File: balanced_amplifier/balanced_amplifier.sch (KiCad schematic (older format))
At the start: 2 parts

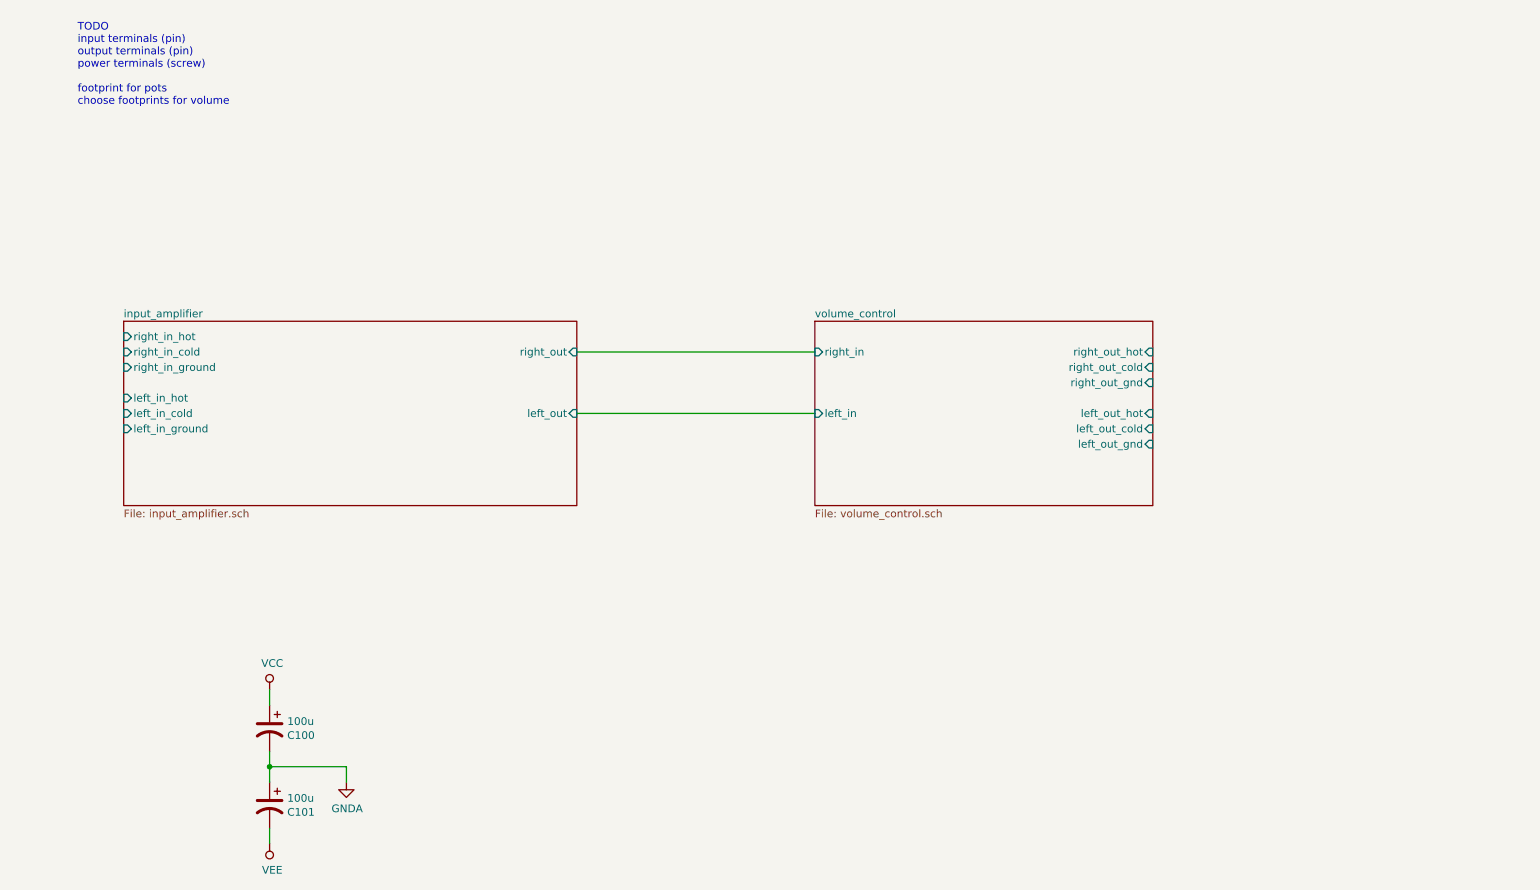
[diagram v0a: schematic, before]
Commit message: Add connectors to root sheet. Connector footprints may need to be changed
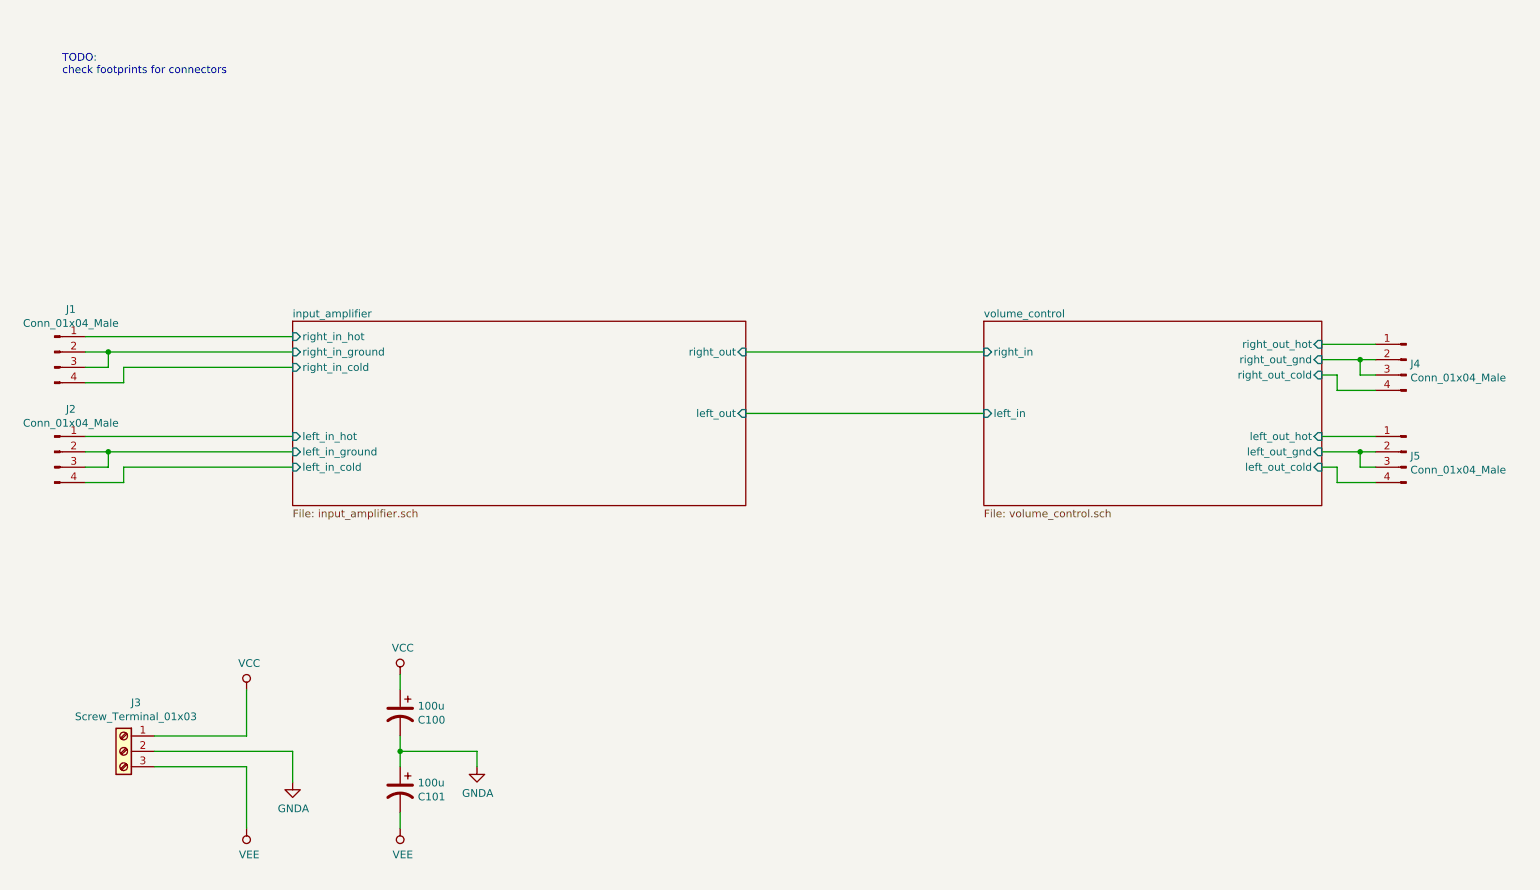
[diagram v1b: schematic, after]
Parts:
- added J1, J2, J4, J5: Conn_01x04_Male, Connector_PinHeader_2.54mm:PinHeader_1x04_P2.54mm_Vertical, symbol Connector:Conn_01x04_Male
- added J3: Screw_Terminal_01x03, TerminalBlock_Phoenix:TerminalBlock_Phoenix_MPT-0,5-3-2.54_1x03_P2.54mm_Horizontal, symbol Connector:Screw_Terminal_01x03
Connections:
- net GNDA: now also J3.2 (Pin_2)
- net VCC: now also J3.1 (Pin_1)
- net VEE: now also J3.3 (Pin_3)
- net input_amplifier/left_in_cold: now also J2.4 (Pin_4)
- net input_amplifier/left_in_ground: now also J2.2 (Pin_2), J2.3 (Pin_3)
- net input_amplifier/left_in_hot: now also J2.1 (Pin_1)
- net input_amplifier/right_in_cold: now also J1.4 (Pin_4)
- net input_amplifier/right_in_ground: now also J1.2 (Pin_2), J1.3 (Pin_3)
- net input_amplifier/right_in_hot: now also J1.1 (Pin_1)
- net volume_control/left_out_cold: now also J5.4 (Pin_4)
- net volume_control/left_out_gnd: now also J5.2 (Pin_2), J5.3 (Pin_3)
- net volume_control/left_out_hot: now also J5.1 (Pin_1)
- net volume_control/right_out_cold: now also J4.4 (Pin_4)
- net volume_control/right_out_gnd: now also J4.2 (Pin_2), J4.3 (Pin_3)
- net volume_control/right_out_hot: now also J4.1 (Pin_1)
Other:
- note added: "TODO:\ncheck footprints for connectors"
- note removed: "TODO\ninput terminals (pin)\noutput terminals (pin)\npower terminals (screw)\n\nfootprint for pots\nchoose footprints for volume"
- moved on the sheet: C100, C101

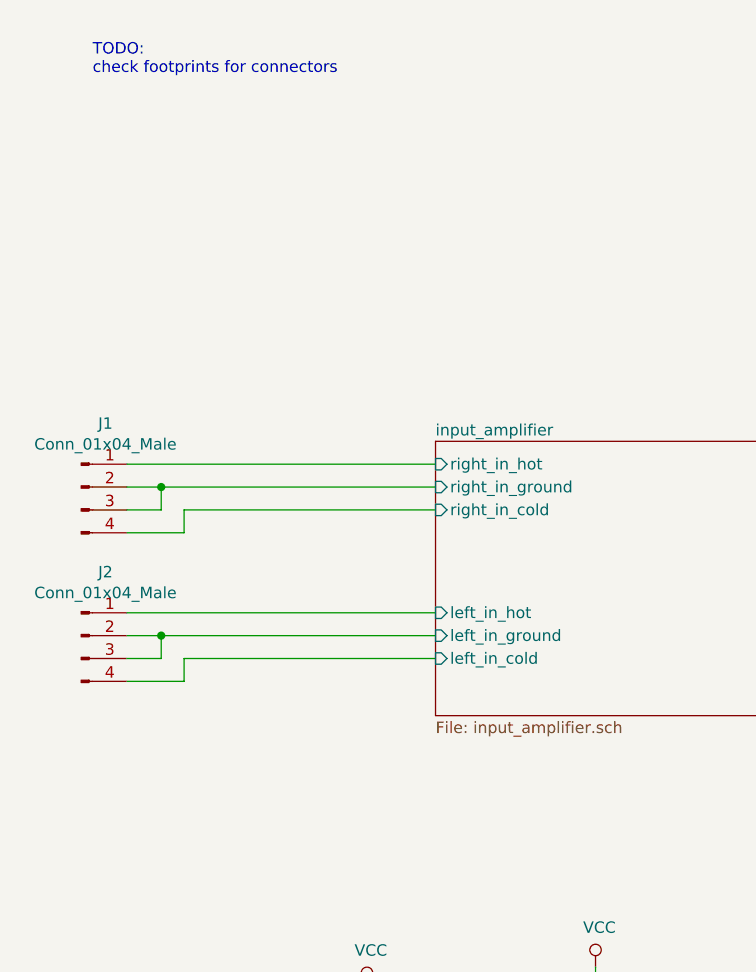
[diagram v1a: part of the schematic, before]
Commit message: swap hot and cold inputs to preserve overall phase
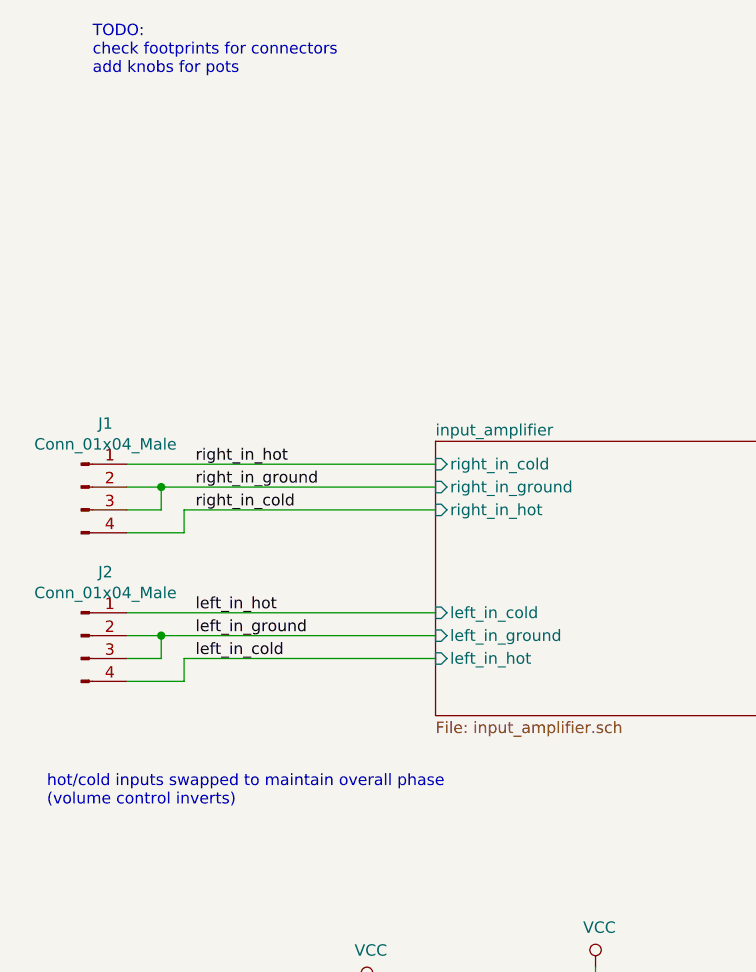
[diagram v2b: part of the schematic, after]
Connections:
- net input_amplifier/left_in_cold renamed left_in_cold
- net input_amplifier/left_in_ground renamed left_in_ground
- net input_amplifier/left_in_hot renamed left_in_hot
- net input_amplifier/right_in_cold renamed right_in_cold
- net input_amplifier/right_in_ground renamed right_in_ground
- net input_amplifier/right_in_hot renamed right_in_hot
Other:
- note added: "TODO:\ncheck footprints for connectors\nadd knobs for pots"
- note added: "hot/cold inputs swapped to maintain overall phase\n(volume control inverts)"
- note removed: "TODO:\ncheck footprints for connectors"
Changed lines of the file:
@@
 F0 "input_amplifier" 50
 F1 "input_amplifier.sch" 50
-F2 "right_in_hot" I L 2500 2600 50
-F3 "right_in_cold" I L 2500 2800 50
+F2 "right_in_hot" I L 2500 2800 50
+F3 "right_in_cold" I L 2500 2600 50
 F4 "right_out" I R 5450 2700 50
-F5 "left_in_hot" I L 2500 3250 50
-F6 "left_in_cold" I L 2500 3450 50
+F5 "left_in_hot" I L 2500 3450 50
+F6 "left_in_cold" I L 2500 3250 50
 F7 "left_out" I R 5450 3100 50
 F8 "right_in_ground" I L 2500 2700 50
@@
 	9300 3450 9200 3450
 Text Notes 1000 900  0    50   ~ 0
-TODO:\ncheck footprints for connectors
+TODO:\ncheck footprints for connectors\nadd knobs for pots
+Text Label 1450 2600 0    50   ~ 0
+right_in_hot
+Text Label 1450 2700 0    50   ~ 0
+right_in_ground
+Text Label 1450 2800 0    50   ~ 0
+right_in_cold
+Text Label 1450 3250 0    50   ~ 0
+left_in_hot
+Text Label 1450 3350 0    50   ~ 0
+left_in_ground
+Text Label 1450 3450 0    50   ~ 0
+left_in_cold
+Text Notes 800  4100 0    50   ~ 0
+hot/cold inputs swapped to maintain overall phase\n(volume control inverts)
 $EndSCHEMATC

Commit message: Update TODO comment
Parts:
- J1, J2: footprint Connector_PinHeader_2.54mm:PinHeader_1x04_P2.54mm_Vertical -> (none); Distributor (none) -> Digikey; Distributor PN (none) -> WM4802-ND; Manufacturer (none) -> Molex; Manufacturer PN (none) -> 0705430003; URL (none) -> https://www.digikey.com/products/en?keywords=0705430003; Unit Price (none) -> 0.99
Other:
- note added: "TODO:\ncreate footprints for shrouded headers (Molex SL)\ncheck footprints for power connector\nadd knobs for pots\nadd testpoints"
- note removed: "TODO:\ncheck footprints for connectors\nadd knobs for pots"
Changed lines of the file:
@@
 F 0 "J1" H 1056 2978 50  0000 C CNN
 F 1 "Conn_01x04_Male" H 1056 2887 50  0000 C CNN
-F 2 "Connector_PinHeader_2.54mm:PinHeader_1x04_P2.54mm_Vertical" H 950 2700 50  0001 C CNN
-F 3 "~" H 950 2700 50  0001 C CNN
+F 2 "" H 950 2700 50  0001 C CNN
+F 3 "https://www.molex.com/pdm_docs/sd/705430001_sd.pdf" H 950 2700 50  0001 C CNN
+F 4 "Molex" H 950 2700 50  0001 C CNN "Manufacturer"
+F 5 "0705430003" H 950 2700 50  0001 C CNN "Manufacturer PN"
+F 6 "Digikey" H 950 2700 50  0001 C CNN "Distributor"
+F 7 "WM4802-ND" H 950 2700 50  0001 C CNN "Distributor PN"
+F 8 "https://www.digikey.com/products/en?keywords=0705430003" H 950 2700 50  0001 C CNN "URL"
+F 9 "0.99" H 950 2700 50  0001 C CNN "Unit Price"
 	1    950  2700
-	1    0    0    -1
-$EndComp
-$Comp
-L Connector:Conn_01x04_Male J2
-U 1 1 5C512DEC
-P 950 3350
-F 0 "J2" H 1056 3628 50  0000 C CNN
-F 1 "Conn_01x04_Male" H 1056 3537 50  0000 C CNN
-F 2 "Connector_PinHeader_2.54mm:PinHeader_1x04_P2.54mm_Vertical" H 950 3350 50  0001 C CNN
-F 3 "~" H 950 3350 50  0001 C CNN
-	1    950  3350
 	1    0    0    -1
 $EndComp
@@
 	9300 3450 9200 3450
 Text Notes 1000 900  0    50   ~ 0
-TODO:\ncheck footprints for connectors\nadd knobs for pots
+TODO:\ncreate footprints for shrouded headers (Molex SL)\ncheck footprints for power connector\nadd knobs for pots\nadd testpoints
 Text Label 1450 2600 0    50   ~ 0
 right_in_hot
@@
 Text Notes 800  4100 0    50   ~ 0
 hot/cold inputs swapped to maintain overall phase\n(volume control inverts)
+$Comp
+L Connector:Conn_01x04_Male J2
+U 1 1 5BFBF6D8
+P 950 3350
+F 0 "J2" H 1056 3628 50  0000 C CNN
+F 1 "Conn_01x04_Male" H 1056 3537 50  0000 C CNN
+F 2 "" H 950 3350 50  0001 C CNN
+F 3 "https://www.molex.com/pdm_docs/sd/705430001_sd.pdf" H 950 3350 50  0001 C CNN
+F 4 "Molex" H 950 3350 50  0001 C CNN "Manufacturer"
+F 5 "0705430003" H 950 3350 50  0001 C CNN "Manufacturer PN"
+F 6 "Digikey" H 950 3350 50  0001 C CNN "Distributor"
+F 7 "WM4802-ND" H 950 3350 50  0001 C CNN "Distributor PN"
+F 8 "https://www.digikey.com/products/en?keywords=0705430003" H 950 3350 50  0001 C CNN "URL"
+F 9 "0.99" H 950 3350 50  0001 C CNN "Unit Price"
+	1    950  3350
+	1    0    0    -1
+$EndComp
 $EndSCHEMATC

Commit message: Update 1x4 connector footprints
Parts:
- J1, J2: footprint (none) -> Connector_Molex_SL:Molex_SL_A-70543-0003_1x04_P2.54mm_Vertical
- J4, J5: footprint Connector_PinHeader_2.54mm:PinHeader_1x04_P2.54mm_Vertical -> Connector_Molex_SL:Molex_SL_A-70543-0003_1x04_P2.54mm_Vertical; Distributor (none) -> Digikey; Distributor PN (none) -> WM4802-ND; Manufacturer (none) -> Molex; Manufacturer PN (none) -> 0705430003; URL (none) -> https://www.digikey.com/products/en?keywords=0705430003; Unit Price (none) -> 0.99
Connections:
- net volume_control/left_out_cold: now also J5.1 (Pin_1); no longer J5.4 (Pin_4)
- net volume_control/left_out_hot: now also J5.4 (Pin_4); no longer J5.1 (Pin_1)
- net volume_control/right_out_cold: now also J4.1 (Pin_1); no longer J4.4 (Pin_4)
- net volume_control/right_out_hot: now also J4.4 (Pin_4); no longer J4.1 (Pin_1)
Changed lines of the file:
@@
 F 0 "J1" H 1056 2978 50  0000 C CNN
 F 1 "Conn_01x04_Male" H 1056 2887 50  0000 C CNN
-F 2 "" H 950 2700 50  0001 C CNN
+F 2 "Connector_Molex_SL:Molex_SL_A-70543-0003_1x04_P2.54mm_Vertical" H 950 2700 50  0001 C CNN
 F 3 "https://www.molex.com/pdm_docs/sd/705430001_sd.pdf" H 950 2700 50  0001 C CNN
 F 4 "Molex" H 950 2700 50  0001 C CNN "Manufacturer"
@@
 	1    950  2700
 	1    0    0    -1
-$EndComp
-$Comp
-L Connector:Conn_01x04_Male J4
-U 1 1 5C512E1C
-P 9750 2750
-F 0 "J4" H 9723 2723 50  0000 R CNN
-F 1 "Conn_01x04_Male" H 9723 2632 50  0000 R CNN
-F 2 "Connector_PinHeader_2.54mm:PinHeader_1x04_P2.54mm_Vertical" H 9750 2750 50  0001 C CNN
-F 3 "~" H 9750 2750 50  0001 C CNN
-	1    9750 2750
-	-1   0    0    -1
-$EndComp
-$Comp
-L Connector:Conn_01x04_Male J5
-U 1 1 5C512E61
-P 9750 3350
-F 0 "J5" H 9723 3323 50  0000 R CNN
-F 1 "Conn_01x04_Male" H 9723 3232 50  0000 R CNN
-F 2 "Connector_PinHeader_2.54mm:PinHeader_1x04_P2.54mm_Vertical" H 9750 3350 50  0001 C CNN
-F 3 "~" H 9750 3350 50  0001 C CNN
-	1    9750 3350
-	-1   0    0    -1
 $EndComp
 $Comp
@@
 F 0 "J2" H 1056 3628 50  0000 C CNN
 F 1 "Conn_01x04_Male" H 1056 3537 50  0000 C CNN
-F 2 "" H 950 3350 50  0001 C CNN
+F 2 "Connector_Molex_SL:Molex_SL_A-70543-0003_1x04_P2.54mm_Vertical" H 950 3350 50  0001 C CNN
 F 3 "https://www.molex.com/pdm_docs/sd/705430001_sd.pdf" H 950 3350 50  0001 C CNN
 F 4 "Molex" H 950 3350 50  0001 C CNN "Manufacturer"
@@
 	1    0    0    -1
 $EndComp
+$Comp
+L Connector:Conn_01x04_Male J4
+U 1 1 5C0E92CC
+P 9750 2850
+F 0 "J4" H 9856 3128 50  0000 C CNN
+F 1 "Conn_01x04_Male" H 9856 3037 50  0000 C CNN
+F 2 "Connector_Molex_SL:Molex_SL_A-70543-0003_1x04_P2.54mm_Vertical" H 9750 2850 50  0001 C CNN
+F 3 "https://www.molex.com/pdm_docs/sd/705430001_sd.pdf" H 9750 2850 50  0001 C CNN
+F 4 "Molex" H 9750 2850 50  0001 C CNN "Manufacturer"
+F 5 "0705430003" H 9750 2850 50  0001 C CNN "Manufacturer PN"
+F 6 "Digikey" H 9750 2850 50  0001 C CNN "Distributor"
+F 7 "WM4802-ND" H 9750 2850 50  0001 C CNN "Distributor PN"
+F 8 "https://www.digikey.com/products/en?keywords=0705430003" H 9750 2850 50  0001 C CNN "URL"
+F 9 "0.99" H 9750 2850 50  0001 C CNN "Unit Price"
+	1    9750 2850
+	-1   0    0    1
+$EndComp
+$Comp
+L Connector:Conn_01x04_Male J5
+U 1 1 5C0E93AE
+P 9750 3450
+F 0 "J5" H 9856 3728 50  0000 C CNN
+F 1 "Conn_01x04_Male" H 9856 3637 50  0000 C CNN
+F 2 "Connector_Molex_SL:Molex_SL_A-70543-0003_1x04_P2.54mm_Vertical" H 9750 3450 50  0001 C CNN
+F 3 "https://www.molex.com/pdm_docs/sd/705430001_sd.pdf" H 9750 3450 50  0001 C CNN
+F 4 "Molex" H 9750 3450 50  0001 C CNN "Manufacturer"
+F 5 "0705430003" H 9750 3450 50  0001 C CNN "Manufacturer PN"
+F 6 "Digikey" H 9750 3450 50  0001 C CNN "Distributor"
+F 7 "WM4802-ND" H 9750 3450 50  0001 C CNN "Distributor PN"
+F 8 "https://www.digikey.com/products/en?keywords=0705430003" H 9750 3450 50  0001 C CNN "URL"
+F 9 "0.99" H 9750 3450 50  0001 C CNN "Unit Price"
+	1    9750 3450
+	-1   0    0    1
+$EndComp
 $EndSCHEMATC

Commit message: Add testpoints
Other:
- note added: "TODO:\ncreate footprints for shrouded headers (Molex SL)\ncheck footprints for power connector\nadd knobs for pots"
- note removed: "TODO:\ncreate footprints for shrouded headers (Molex SL)\ncheck footprints for power connector\nadd knobs for pots\nadd testpoints"
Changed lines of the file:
@@
 	9300 3450 9200 3450
 Text Notes 1000 900  0    50   ~ 0
-TODO:\ncreate footprints for shrouded headers (Molex SL)\ncheck footprints for power connector\nadd knobs for pots\nadd testpoints
+TODO:\ncreate footprints for shrouded headers (Molex SL)\ncheck footprints for power connector\nadd knobs for pots
 Text Label 1450 2600 0    50   ~ 0
 right_in_hot

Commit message: Update power connector part information, footprint
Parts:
- J3: footprint TerminalBlock_Phoenix:TerminalBlock_Phoenix_MPT-0,5-3-2.54_1x03_P2.54mm_Horizontal -> TerminalBlock_Phoenix:TerminalBlock_Phoenix_PT-1,5-3-5.0-H_1x03_P5.00mm_Horizontal; Distributor (none) -> Digikey; Distributor PN (none) -> 277-1578-ND; Manufacturer (none) -> Phoenix; Manufacturer PN (none) -> 1935174; URL (none) -> https://www.digikey.com/product-detail/en/phoenix-contact/1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; Unit Price (none) -> 0.60
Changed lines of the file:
@@
 F 0 "J3" H 1320 5617 50  0000 C CNN
 F 1 "Screw_Terminal_01x03" H 1320 5526 50  0000 C CNN
-F 2 "TerminalBlock_Phoenix:TerminalBlock_Phoenix_MPT-0,5-3-2.54_1x03_P2.54mm_Horizontal" H 1400 5300 50  0001 C CNN
-F 3 "~" H 1400 5300 50  0001 C CNN
+F 2 "TerminalBlock_Phoenix:TerminalBlock_Phoenix_PT-1,5-3-5.0-H_1x03_P5.00mm_Horizontal" H 1400 5300 50  0001 C CNN
+F 3 "https://media.digikey.com/pdf/Data%20Sheets/Phoenix%20Contact%20PDFs/1935174.pdf" H 1400 5300 50  0001 C CNN
+F 4 "Phoenix" H 1400 5300 50  0001 C CNN "Manufacturer"
+F 5 "1935174" H 1400 5300 50  0001 C CNN "Manufacturer PN"
+F 6 "Digikey" H 1400 5300 50  0001 C CNN "Distributor"
+F 7 "277-1578-ND" H 1400 5300 50  0001 C CNN "Distributor PN"
+F 8 "https://www.digikey.com/product-detail/en/phoenix-contact/1935174/277-1578-ND/568615" H 1400 5300 50  0001 C CNN "URL"
+F 9 "0.60" H 1400 5300 50  0001 C CNN "Unit Price"
 	1    1400 5300
 	-1   0    0    -1

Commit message: Add power flags, run DRC
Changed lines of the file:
@@
 $EndComp
 Wire Wire Line
-	2200 5800 2200 5400
+	2200 5800 2200 5500
 Wire Wire Line
 	2200 5400 1600 5400
@@
 	-1   0    0    1
 $EndComp
+$Comp
+L power:PWR_FLAG #FLG?
+U 1 1 5C227712
+P 2200 5200
+F 0 "#FLG?" H 2200 5275 50  0001 C CNN
+F 1 "PWR_FLAG" V 2200 5328 50  0000 L CNN
+F 2 "" H 2200 5200 50  0001 C CNN
+F 3 "~" H 2200 5200 50  0001 C CNN
+	1    2200 5200
+	0    1    1    0
+$EndComp
+Connection ~ 2500 5300
+Connection ~ 2200 5200
+$Comp
+L power:PWR_FLAG #FLG?
+U 1 1 5C22777E
+P 2500 5300
+F 0 "#FLG?" H 2500 5375 50  0001 C CNN
+F 1 "PWR_FLAG" V 2500 5428 50  0000 L CNN
+F 2 "" H 2500 5300 50  0001 C CNN
+F 3 "~" H 2500 5300 50  0001 C CNN
+	1    2500 5300
+	0    1    1    0
+$EndComp
+$Comp
+L power:PWR_FLAG #FLG?
+U 1 1 5C227797
+P 2200 5500
+F 0 "#FLG?" H 2200 5575 50  0001 C CNN
+F 1 "PWR_FLAG" V 2200 5628 50  0000 L CNN
+F 2 "" H 2200 5500 50  0001 C CNN
+F 3 "~" H 2200 5500 50  0001 C CNN
+	1    2200 5500
+	0    -1   1    0
+$EndComp
+Connection ~ 2200 5500
+Wire Wire Line
+	2200 5500 2200 5400
 $EndSCHEMATC
